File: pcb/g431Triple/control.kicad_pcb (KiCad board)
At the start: 2 copper layers, 64 x 39.5 mm, 60 parts, among them J1 USB_C_Receptacle_USB2.0, P1 FTSH-107-01-L-DV-K, P2 ST-Link, P3 AFC07-S24FCC-00, P4 har-flexicon 2,54 MSH-4, P5 har-flexicon 2,54 MSH-4, P6 har-flexicon 2,54 MSH-4, P7 WAGO2061-602, P8 WAGO2061-602, P9 WAGO2061-602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

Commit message: Rename to g431/g431Triple, new pin ordering for Harting connector
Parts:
- added JP5: Jumper_2_Open, local:Jumper, F.Cu at (81.4, 108.8)
- added JP6: Jumper_2_Open, local:Jumper, F.Cu at (109.9, 108.5)
- added JP7: Jumper_2_Open, local:Jumper, F.Cu at (123.8, 109.4)
- J1: value USB_C_Receptacle_USB2.0 -> TYPE-C 16PIN 2MD(073)
- moved D5 25.9 mm to (109.9, 108.5)
- moved D6 5.85 mm to (123.8, 109.4)
- moved D4 4.28 mm to (81.4, 108.8)
- moved R12 4.20 mm to (77.2, 108.7)
- moved R16 3.90 mm to (119.6, 108.4)
- moved R13 2.00 mm to (89.7, 104.8)
- moved R14 2.00 mm to (87.7, 104.8)
- moved R9 0.75 mm to (117.8, 112.8)
- moved C17 0.60 mm to (113.9, 105.9)
- moved U6 0.59 mm to (113.7, 110.2)
- moved C3 0.50 mm to (110.6, 115.7)
- moved R7 0.39 mm to (89.1, 114.4), turned to 180 degrees
- moved R11 0.20 mm to (79.2, 108.7)
- moved P4 0.10 mm to (77.0, 102.2), turned to 180 degrees
- moved P5 0.10 mm to (100.0, 102.2), turned to 180 degrees
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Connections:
- net RS485_A renamed RS485_1_A
- net RS485_B renamed RS485_1_B
- net RS485_DE renamed RS485_1_DE
- net RS485_RX renamed RS485_1_RX
- net RS485_TX renamed RS485_1_TX
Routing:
- net GND: track 372.8 -> 430.9 mm, vias 25 -> 28
- net Net-(D5-A): track 64.0 -> 45.8 mm
- net Net-(D6-A): track 34.2 -> 25.8 mm
- net +15V: track 93.4 -> 85.3 mm, vias 5 -> 6
- net RS485_2_A: track 17.3 -> 10.3 mm
- net +3V3: track 255.7 -> 259.6 mm
- net Net-(U4-B): track 10.6 -> 6.74 mm
- net Net-(U5-B): track 5.49 -> 2.02 mm
- net RS485_2_B: track 16.4 -> 13.5 mm
- net Net-(U6-B): track 11.7 -> 8.84 mm
- net Net-(U6-A): track 7.80 -> 9.57 mm
- net RS485_1_B: track 6.09 -> 7.65 mm
- net RS485_3_B: track 6.79 -> 5.27 mm
- net Net-(D4-A): track 29.6 -> 30.8 mm
- net RS485_3_A: track 6.45 -> 5.32 mm
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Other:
- board text added: "VBUS"

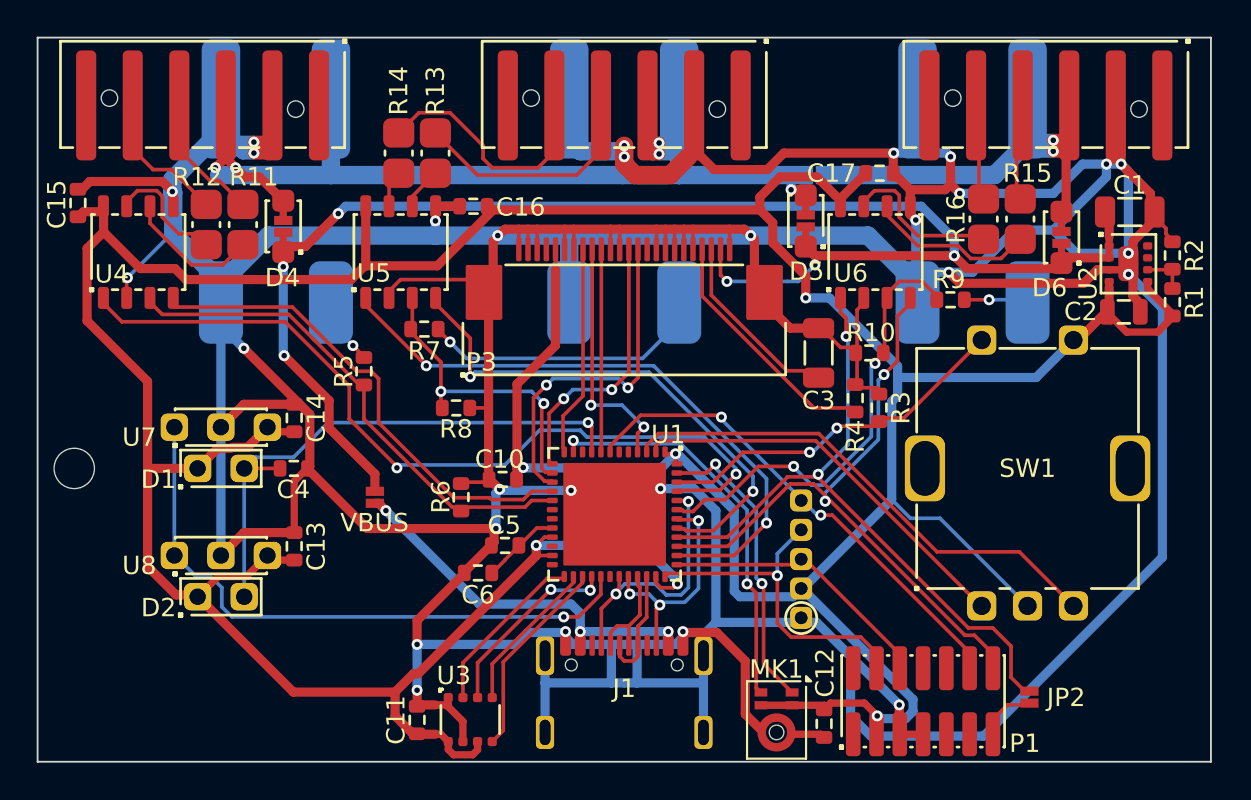
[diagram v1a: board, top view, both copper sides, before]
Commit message: Multiple led strips
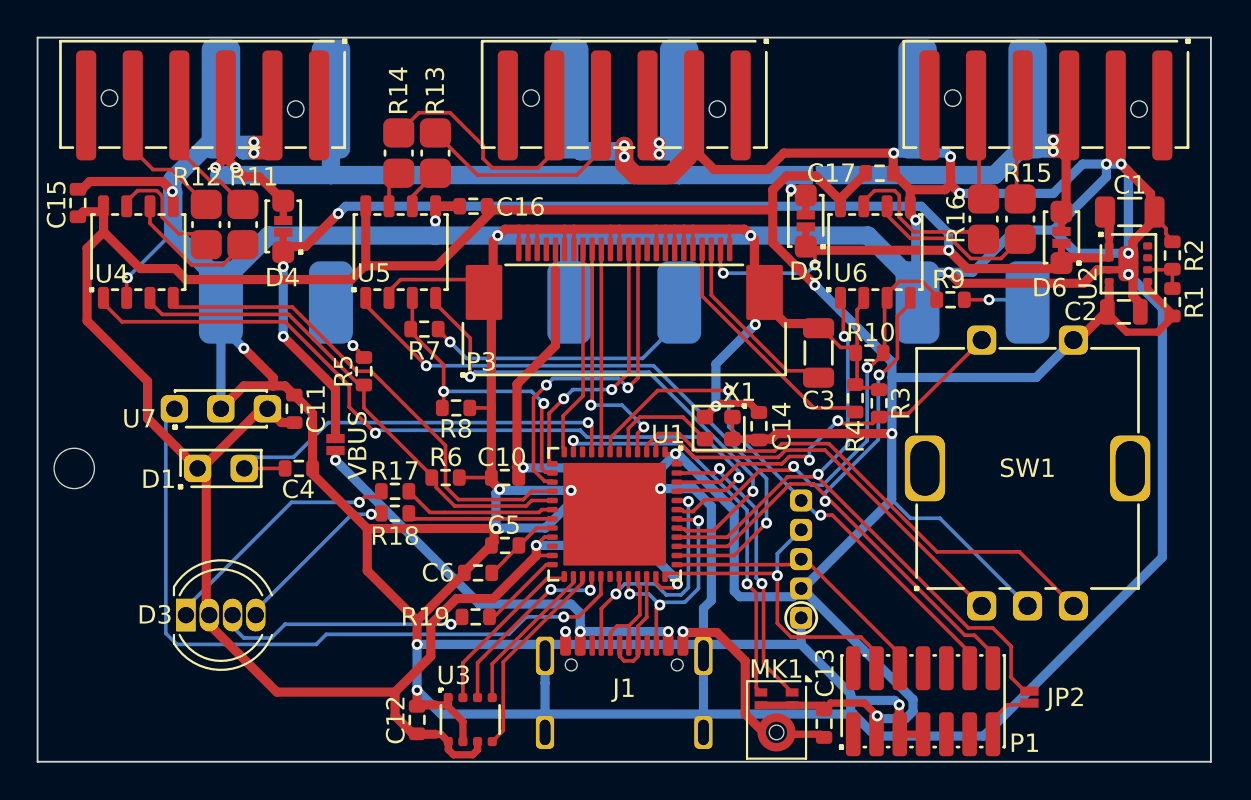
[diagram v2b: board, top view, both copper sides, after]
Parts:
- removed D2: D_Photo, local:PhotoDiode
- removed U8: TSOP38338, local:TSOP38338
- added D3: LED_RABG, LED_THT:LED_D5.0mm-4_RGB, F.Cu at (76.1, 130.0)
- added R17: 1k, local:0603, F.Cu at (87.5, 123.2)
- added R18: 470R, local:0603, F.Cu at (87.5, 124.5)
- added R19: 330R, local:0603, F.Cu at (91.9, 130.1)
- added X1: O24.000000-JSO21C1LC-D-3.3-T3-N-0, local:JSO21, F.Cu at (105.2, 119.8)
- moved C14 25.4 mm to (107.3, 119.7)
- moved C11 7.50 mm to (82.0, 118.8)
- moved JP1 3.59 mm to (84.2, 120.7)
- moved R6 1.37 mm to (90.2, 122.5), turned to 0 degrees
- moved U7 1.00 mm to (78.0, 118.2)
- moved C4 0.28 mm to (82.2, 122.0)
- moved R3 0.24 mm to (113.9, 118.5)
- moved C10 0.16 mm to (93.5, 122.5)
- renumbered C13 to C11, C11 to C12, C12 to C13
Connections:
- U1 pad 18: unconnected-(U1-PB1-Pad18) -> LED_R
- U1 pad 19: unconnected-(U1-PB2-Pad19) -> LED_G
- U1 pad 24: unconnected-(U1-PB11-Pad24) -> LED_B
- U1 pad 5: unconnected-(U1-PF0-Pad5) -> OSC24
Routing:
- net GND: track 430.9 -> 448.9 mm, vias 28 -> 30
- net Net-(D3-BK): track 0.00 -> 13.9 mm, vias 0 -> 1
- net Net-(D3-RK): track 0.00 -> 13.7 mm, vias 0 -> 1
- net Net-(D3-GK): track 0.00 -> 9.29 mm, vias 0 -> 1
- net LED_R: track 0.00 -> 8.36 mm
- net LED_G: track 0.00 -> 7.95 mm
- net BS: track 30.4 -> 23.7 mm
- net OSC24: track 0.00 -> 6.21 mm
- net +15V: track 85.3 -> 80.5 mm
- net IR: track 33.8 -> 38.5 mm
- net LED_B: track 0.00 -> 4.57 mm
- net VBUS: track 21.3 -> 25.0 mm
- net nRST: track 27.1 -> 29.5 mm
- net +3V3: track 259.6 -> 261.4 mm, vias 6 -> 7
- net RS485_1_RX: track 45.3 -> 43.6 mm
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
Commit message: Add color temperature
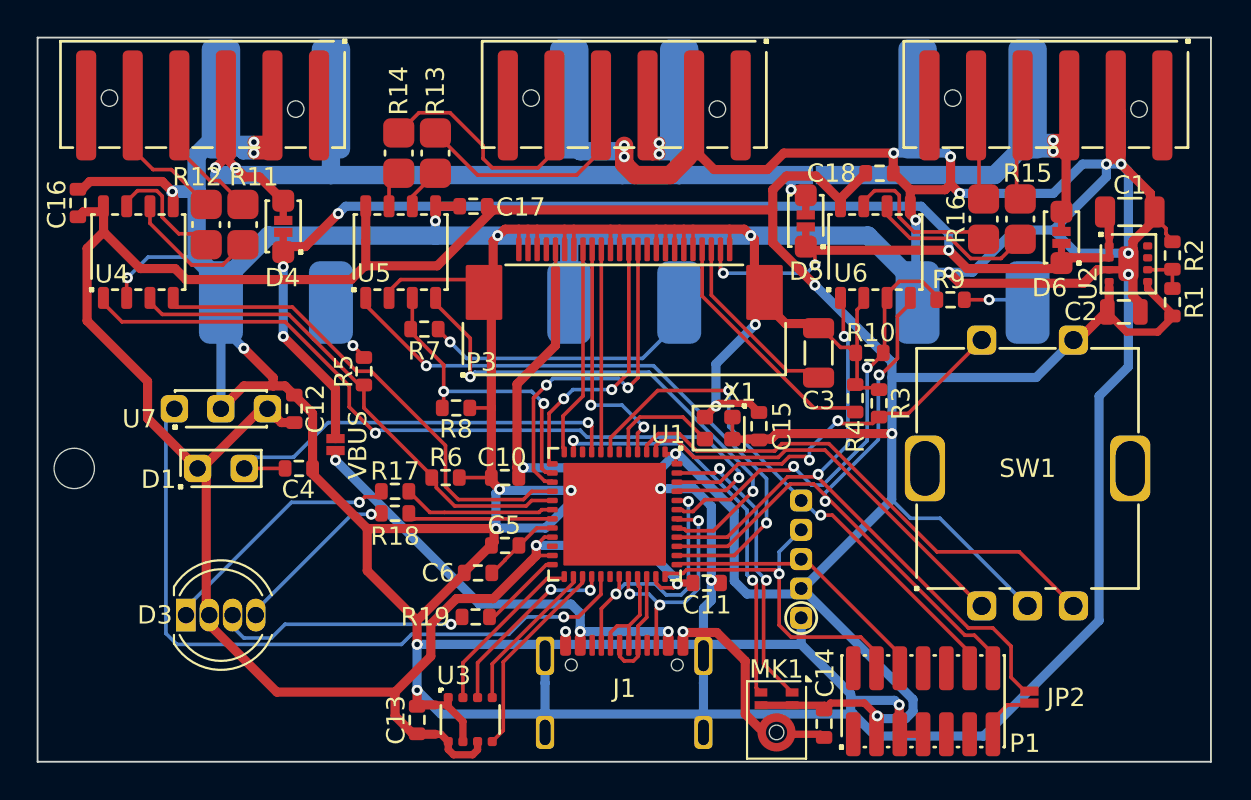
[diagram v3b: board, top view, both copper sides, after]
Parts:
- added C12: 100n, local:0603, F.Cu at (82.0, 118.8)
- moved C11 24.4 mm to (104.5, 128.2), turned to 0 degrees
- renumbered C12 to C13, C13 to C14, C14 to C15, C15 to C16, C16 to C17, C17 to C18
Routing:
- net GND: track 448.9 -> 448.5 mm, vias 30 -> 31

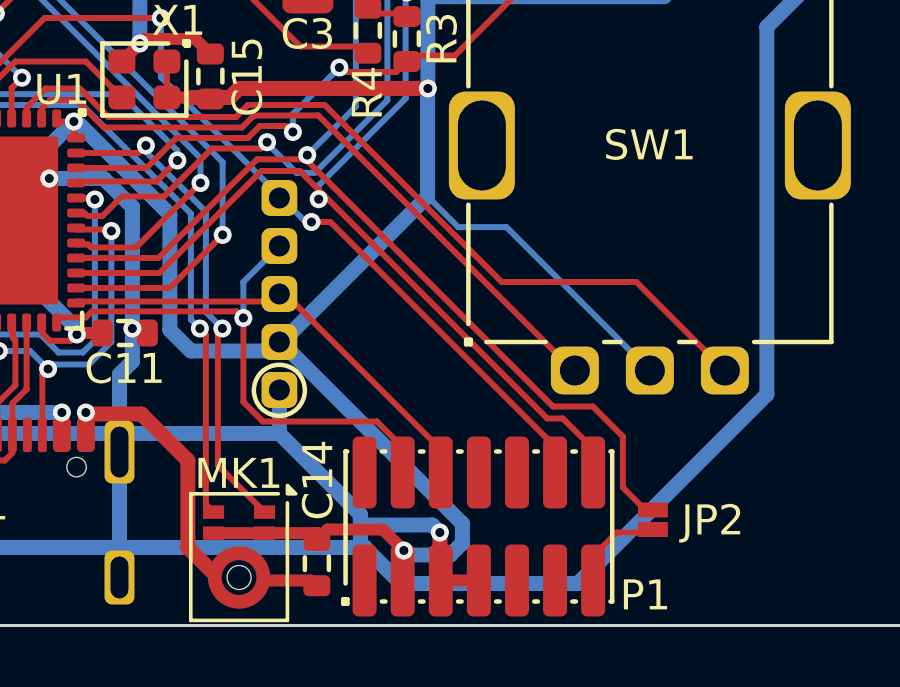
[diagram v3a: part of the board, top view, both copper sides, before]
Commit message: Start preset name editor
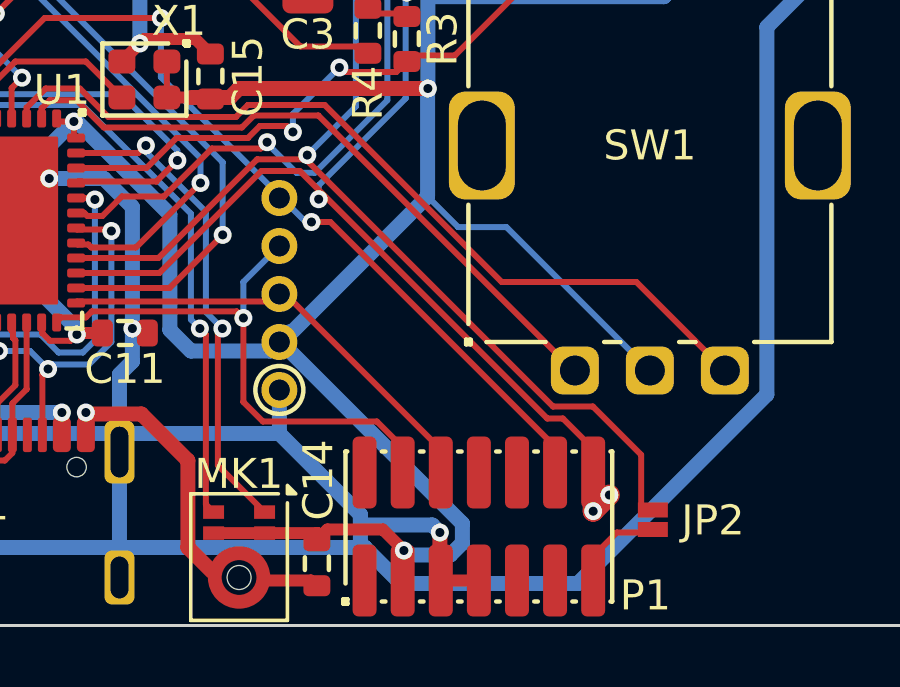
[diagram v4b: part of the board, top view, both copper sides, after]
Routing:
- net RS485_3_TX: track 36.4 -> 38.4 mm, vias 2 -> 4
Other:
- board text added: "GND"

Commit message: Works on g431Triple
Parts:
- moved D5 0.05 mm to (109.8, 108.5)
